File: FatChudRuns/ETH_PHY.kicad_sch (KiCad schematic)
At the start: 55 parts, among them J1 RJ45_Pulse_JXD6-0001NL, U2 DP83848I

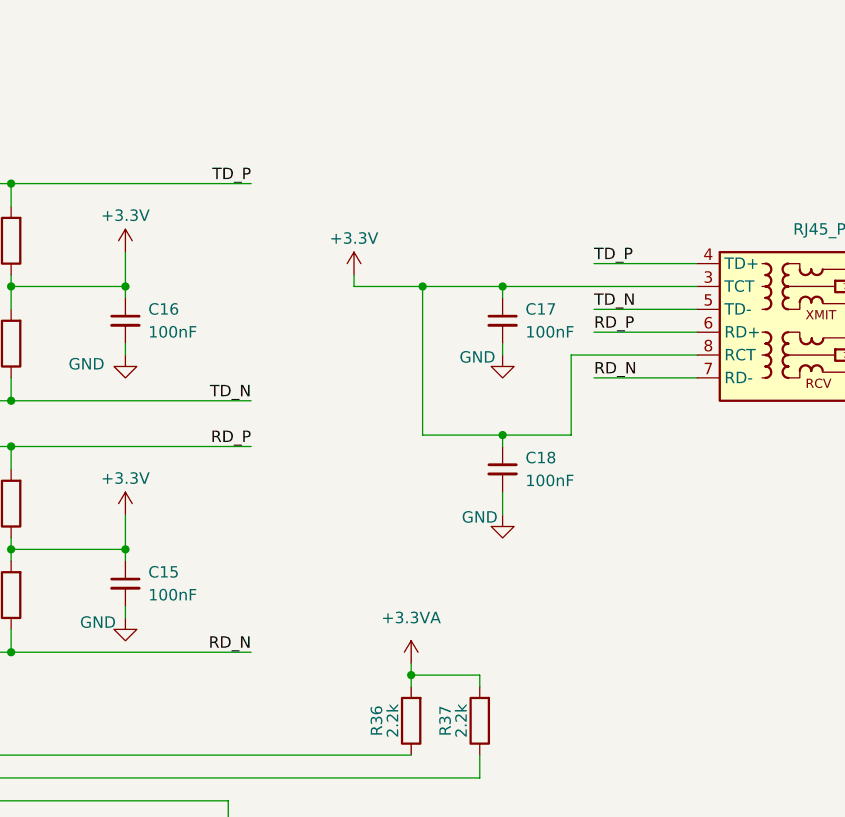
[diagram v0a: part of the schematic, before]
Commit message: added 4pF caps and Rext to XTAL, initial placement of PCB, added board outline and gnd plane
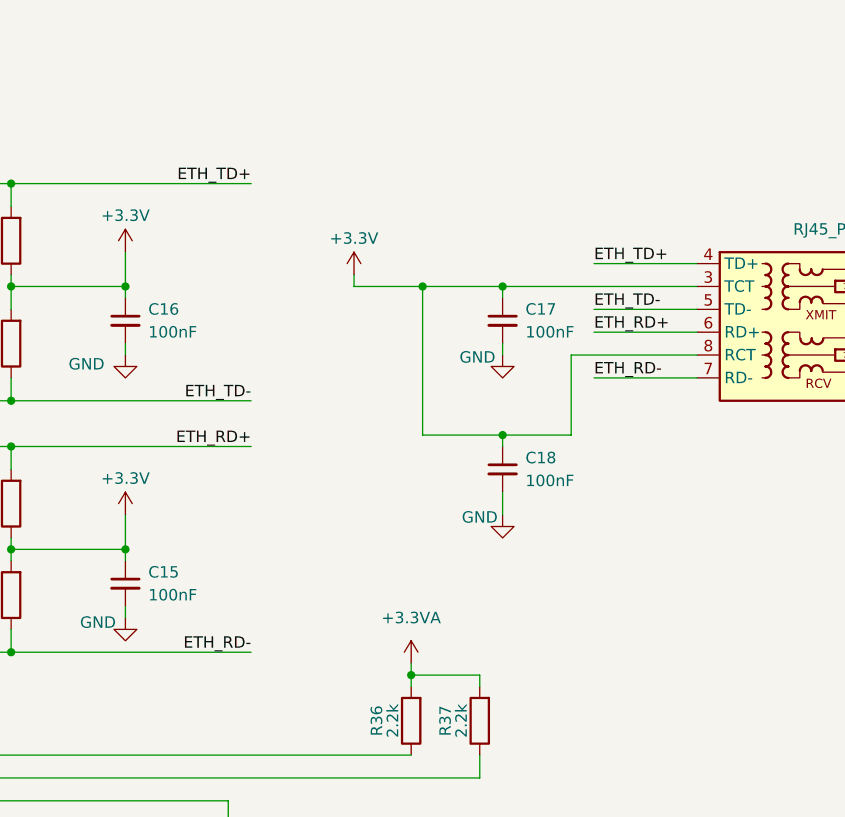
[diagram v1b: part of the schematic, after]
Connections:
- net RD_N renamed ETH_RD-
- net RD_P renamed ETH_RD+
- net TD_N renamed ETH_TD-
- net TD_P renamed ETH_TD+
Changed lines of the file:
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@@
 		)
 	)
-	(label "TD_N"
+	(label "ETH_TD-"
 		(at 323.85 83.82 0)
 		(effects
@@
 		)
 	)
-	(label "RD_P"
+	(label "ETH_RD+"
 		(at 323.85 86.36 0)
 		(effects
@@
 		)
 	)
-	(label "TD_N"
+	(label "ETH_TD-"
 		(at 285.75 93.98 180)
 		(effects
@@
 		)
 	)
-	(label "RD_P"
+	(label "ETH_RD+"
 		(at 285.75 99.06 180)
 		(effects
@@
 		)
 	)
-	(label "TD_P"
+	(label "ETH_TD+"
 		(at 323.85 78.74 0)
 		(effects
@@
 		)
 	)
-	(label "RD_N"
+	(label "ETH_RD-"
 		(at 285.75 121.92 180)
 		(effects
@@
 		)
 	)
-	(label "RD_N"
+	(label "ETH_RD-"
 		(at 323.85 91.44 0)
 		(effects
@@
 		)
 	)
-	(label "TD_P"
+	(label "ETH_TD+"
 		(at 285.75 69.85 180)
-		(effects
-			(font
-				(size 1.27 1.27)
-			)
-			(justify right bottom)
-		)
-	)
+		(fields_autoplaced yes)
+		(effects
+			(font
+				(size 1.27 1.27)
+			)
+			(justify right bottom)
+		)
+		(property "ETH_DP100" ""
+			(at 285.75 71.12 0)
+			(effects
+				(font
+					(size 1.27 1.27)
+					(italic yes)
+				)
+				(justify right)
+			)
+		)
+	)

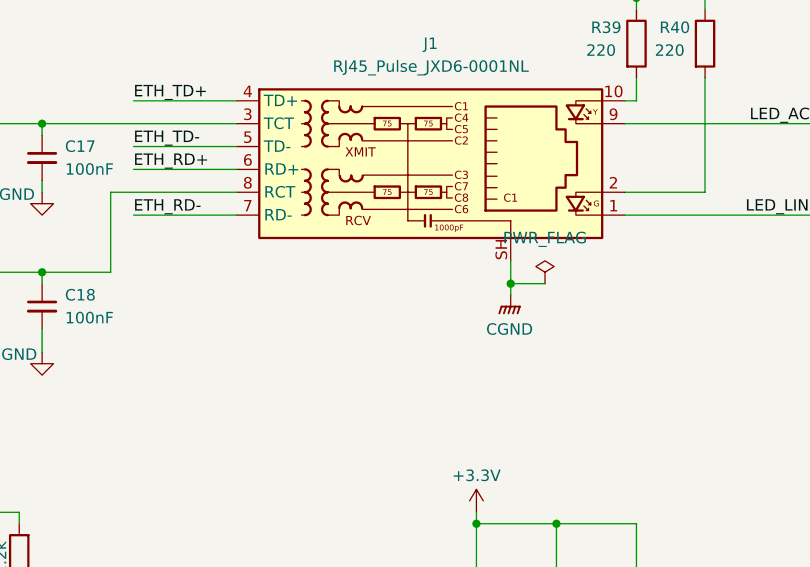
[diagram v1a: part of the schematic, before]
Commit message: routed ETH MDI and magnetics portion with chassis ground. added 0ohm resistors to connect gnd and cgnd
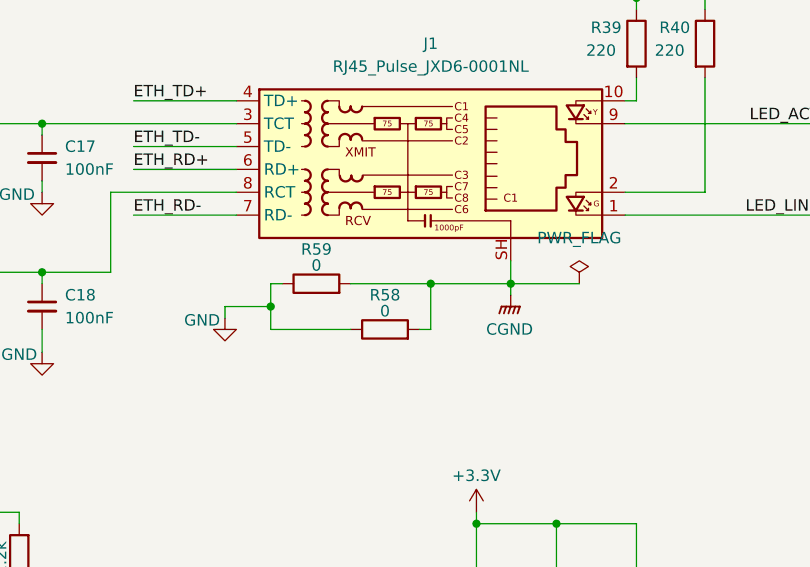
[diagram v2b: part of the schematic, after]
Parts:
- added R58, R59: 0, Resistor_SMD:R_0603_1608Metric, symbol Device:R
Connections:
- net CGND: now also R58.2, R59.2
- net GND: now also R58.1, R59.1

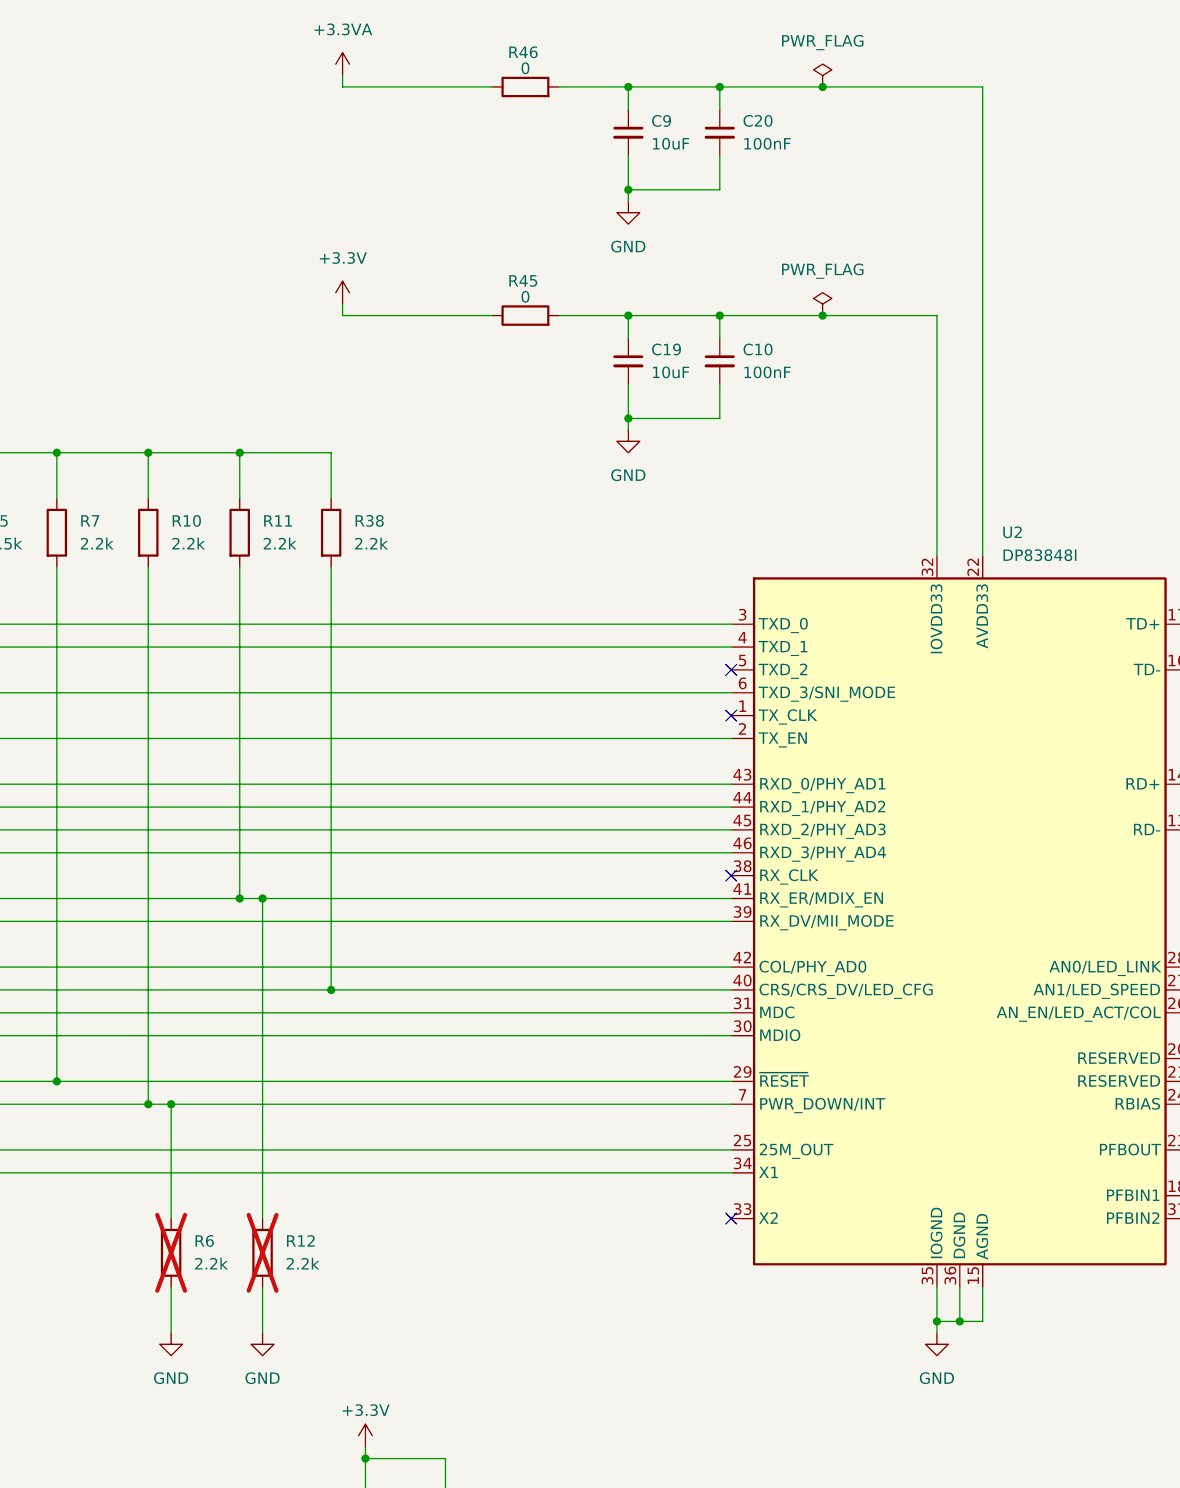
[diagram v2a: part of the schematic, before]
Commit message: added one more decoup cap for eth phy (another power pin), routed decoup caps, routed phy filter resistors
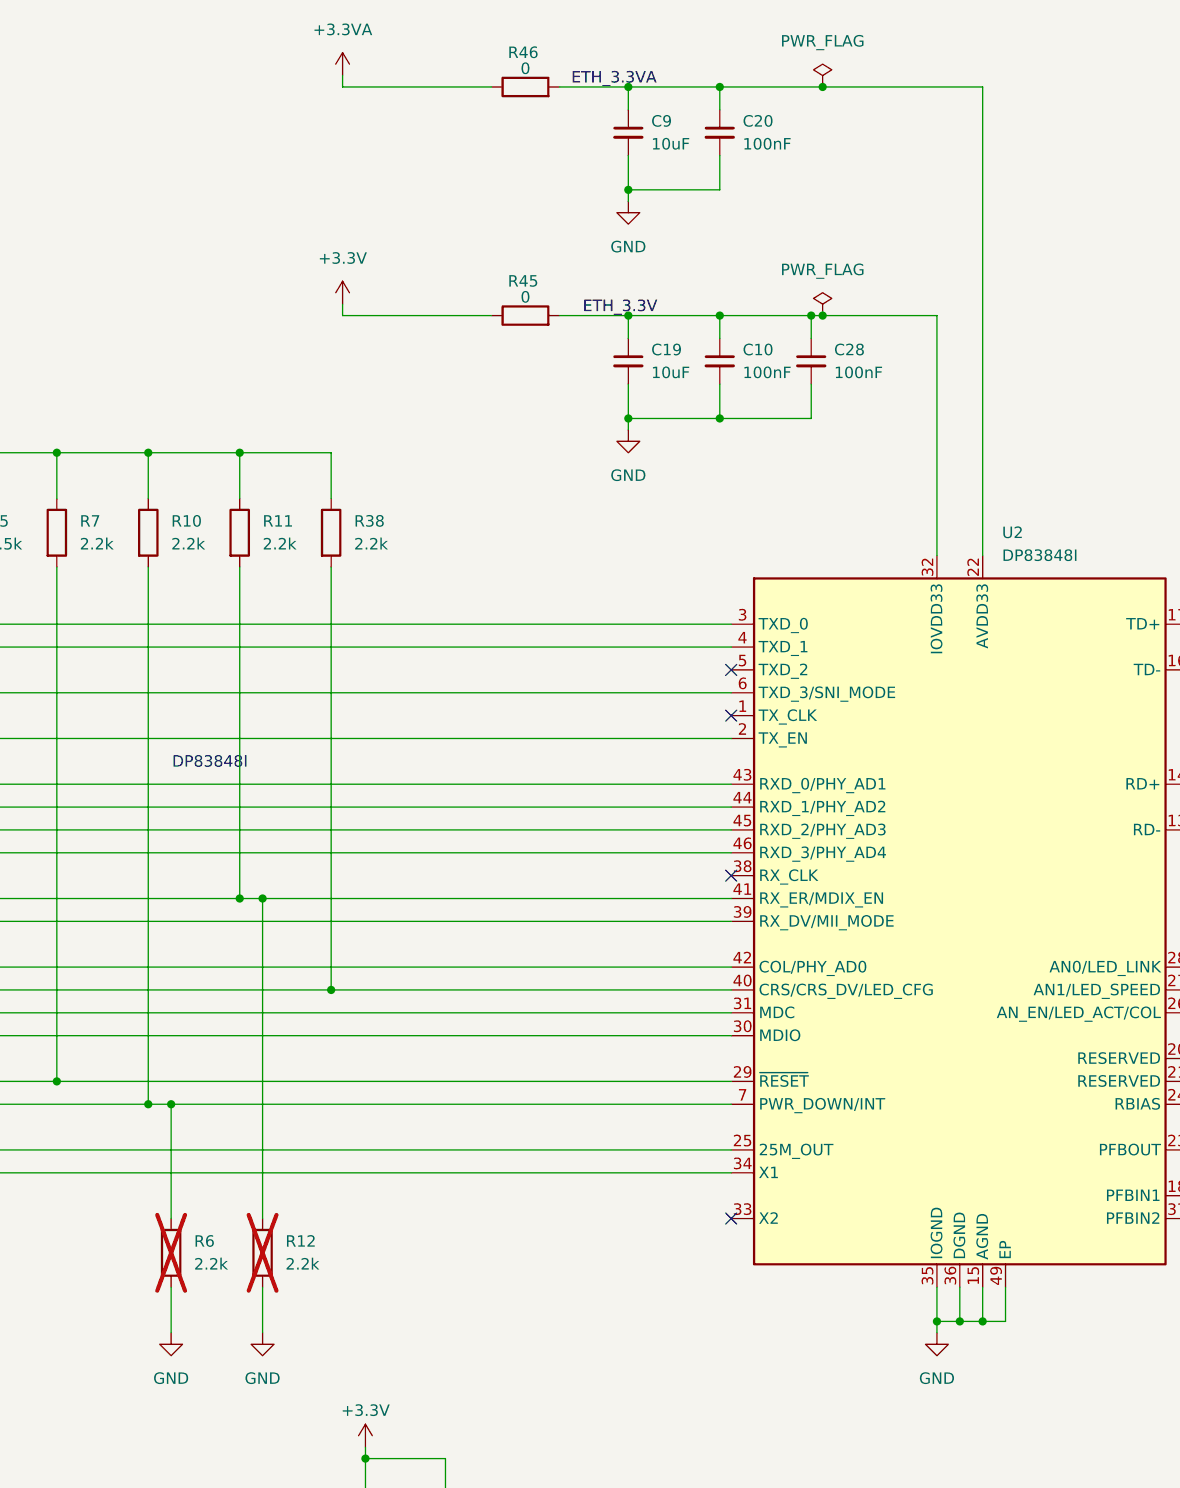
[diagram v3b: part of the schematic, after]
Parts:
- added C28: 100nF, Capacitor_SMD:C_0603_1608Metric, symbol Device:C_Small
- U2: footprint Package_QFP:LQFP-48_7x7mm_P0.5mm -> Package_QFP:LQFP-48-1EP_7x7mm_P0.5mm_EP3.6x3.6mm_ThermalVias
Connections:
- net GND: now also U2.49 (EP), C28.2
- net ETH_3.3VA: now reaches C20.1, C9.1, R46.2, U2.22 (AVDD33)
- net ETH_3.3V: now reaches C10.1, C19.1, R45.2, U2.32 (IOVDD33), U2.48 (IOVDD33)
- net ETH_3.3V: now also C28.1
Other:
- note added: "DP83848I"
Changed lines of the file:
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@@
 		)
 	)
+	(text "DP83848I"
+		(exclude_from_sim no)
+		(at 118.618 100.584 0)
+		(effects
+			(font
+				(size 1.27 1.27)
+			)
+		)
+	)
 	(junction
 		(at 361.95 125.73)
@@
 	)
 	(junction
+		(at 175.26 62.23)
+		(diameter 0)
+		(color 0 0 0 0)
+	)
+	(junction
 		(at 256.54 171.45)
 		(diameter 0)
@@
 	)
 	(junction
+		(at 185.42 50.8)
+		(diameter 0)
+		(color 0 0 0 0)
+	)
+	(junction
 		(at 114.3 138.43)
 		(diameter 0)
@@
 	)
 	(junction
+		(at 204.47 162.56)
+		(diameter 0)
+		(color 0 0 0 0)
+	)
+	(junction
 		(at 68.58 185.42)
 		(diameter 0)
@@
 	(wire
 		(pts
+			(xy 207.01 158.75) (xy 207.01 162.56)
+		)
+		(stroke
+			(width 0)
+			(type default)
+		)
+	)
+	(wire
+		(pts
 			(xy 232.41 148.59) (xy 232.41 151.13)
 		)
@@
 	(wire
 		(pts
+			(xy 185.42 50.8) (xy 186.69 50.8)
+		)
+		(stroke
+			(width 0)
+			(type default)
+		)
+	)
+	(wire
+		(pts
 			(xy 144.78 177.8) (xy 144.78 184.15)
 		)
@@
 	(wire
 		(pts
+			(xy 204.47 162.56) (xy 207.01 162.56)
+		)
+		(stroke
+			(width 0)
+			(type default)
+		)
+	)
+	(wire
+		(pts
 			(xy 227.33 125.73) (xy 240.03 125.73)
 		)
@@
 	(wire
 		(pts
-			(xy 175.26 50.8) (xy 186.69 50.8)
+			(xy 175.26 50.8) (xy 185.42 50.8)
 		)
 		(stroke
@@
 	(wire
 		(pts
+			(xy 175.26 62.23) (xy 185.42 62.23)
+		)
+		(stroke
+			(width 0)
+			(type default)
+		)
+	)
+	(wire
+		(pts
 			(xy 101.6 135.89) (xy 176.53 135.89)
 		)
@@
 	(wire
 		(pts
+			(xy 185.42 62.23) (xy 185.42 58.42)
+		)
+		(stroke
+			(width 0)
+			(type default)
+		)
+	)
+	(wire
+		(pts
 			(xy 91.44 64.77) (xy 91.44 66.04)
 		)
@@
 	(wire
 		(pts
+			(xy 185.42 50.8) (xy 185.42 53.34)
+		)
+		(stroke
+			(width 0)
+			(type default)
+		)
+	)
+	(wire
+		(pts
 			(xy 242.57 99.06) (xy 259.08 99.06)
 		)
@@
 		)
 	)
+	(label "ETH_3.3V"
+		(at 160.02 50.8 0)
+		(effects
+			(font
+				(size 1.27 1.27)
+			)
+			(justify left bottom)
+		)
+	)
 	(label "ETH_TD-"
 		(at 323.85 83.82 0)
@@
 		)
 	)
+	(label "ETH_3.3VA"
+		(at 158.75 25.4 0)
+		(effects
+			(font
+				(size 1.27 1.27)
+			)
+			(justify left bottom)
+		)
+	)
 	(label "PHY_AD4"
 		(at 64.77 110.49 0)
@@
 	)
 	(symbol
+		(lib_id "Device:C_Small")
+		(at 185.42 55.88 0)
+		(unit 1)
+		(exclude_from_sim no)
+		(in_bom yes)
+		(on_board yes)
+		(dnp no)
+		(fields_autoplaced yes)
+		(property "Reference" "C28"
+			(at 187.96 54.6162 0)
+			(effects
+				(font
+					(size 1.27 1.27)
+				)
+				(justify left)
+			)
+		)
+		(property "Value" "100nF"
+			(at 187.96 57.1562 0)
+			(effects
+				(font
+					(size 1.27 1.27)
+				)
+				(justify left)
+			)
+		)
+		(property "Footprint" "Capacitor_SMD:C_0603_1608Metric"
+			(at 185.42 55.88 0)
+			(effects
+				(font
+					(size 1.27 1.27)
+				)
+				(hide yes)
+			)
+		)
+		(property "Datasheet" "~"
+			(at 185.42 55.88 0)
+			(effects
+				(font
+					(size 1.27 1.27)
+				)
+				(hide yes)
+			)
+		)
+		(property "Description" "Unpolarized capacitor, small symbol"
+			(at 185.42 55.88 0)
+			(effects
+				(font
+					(size 1.27 1.27)
+				)
+				(hide yes)
+			)
+		)
+		(pin "1"
+		)
+		(pin "2"
+		)
+		(instances
+			(project "FatChudRuns"
+				(path "/8ed38441-7d4e-4e89-870f-07e11c6dce38/38bcdc9d-582a-45a7-b0b4-f0014b983161"
+					(reference "C28")
+					(unit 1)
+				)
+			)
+		)
+	)
+	(symbol
 		(lib_id "power:+3.3V")
 		(at 133.35 49.53 0)
@@
 			)
 		)
-		(property "Footprint" "Package_QFP:LQFP-48_7x7mm_P0.5mm"
+		(property "Footprint" "Package_QFP:LQFP-48-1EP_7x7mm_P0.5mm_EP3.6x3.6mm_ThermalVias"
 			(at 227.33 157.48 0)
 			(effects
@@
 		(pin "7"
 		)
+		(pin "49"
+		)
 		(instances
